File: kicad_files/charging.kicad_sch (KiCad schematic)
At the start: 40 parts, among them Q1 AO3400A, Q2 AO3400A, Q3 AO3401A, Q5 Q_PMOS, Q6 AO3401A, U2 BQ24172RGYR, U3 CYPD3177-24LQ

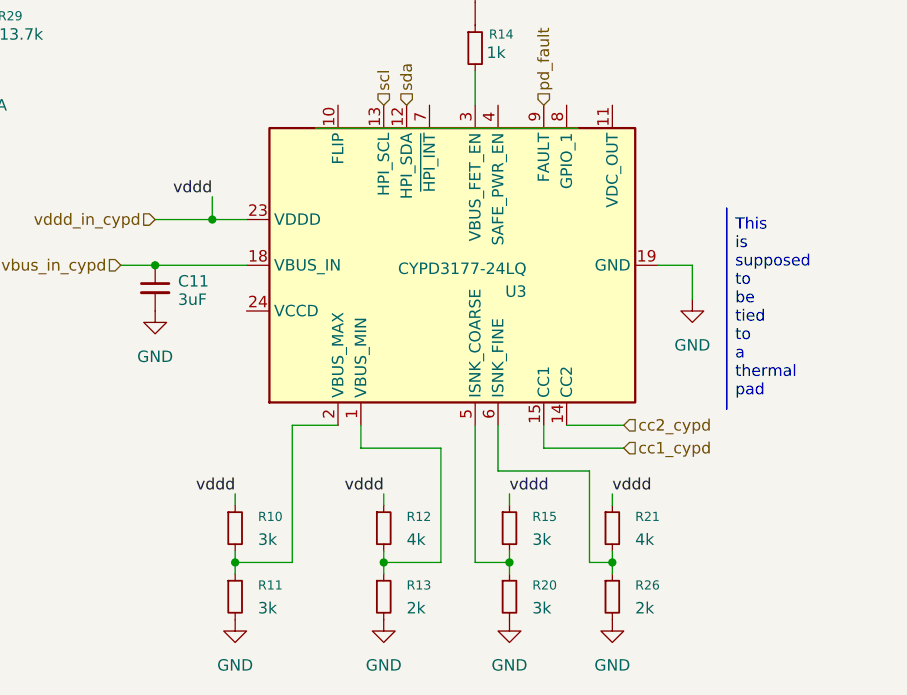
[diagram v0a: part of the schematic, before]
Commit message: fixed some labels and added some passives
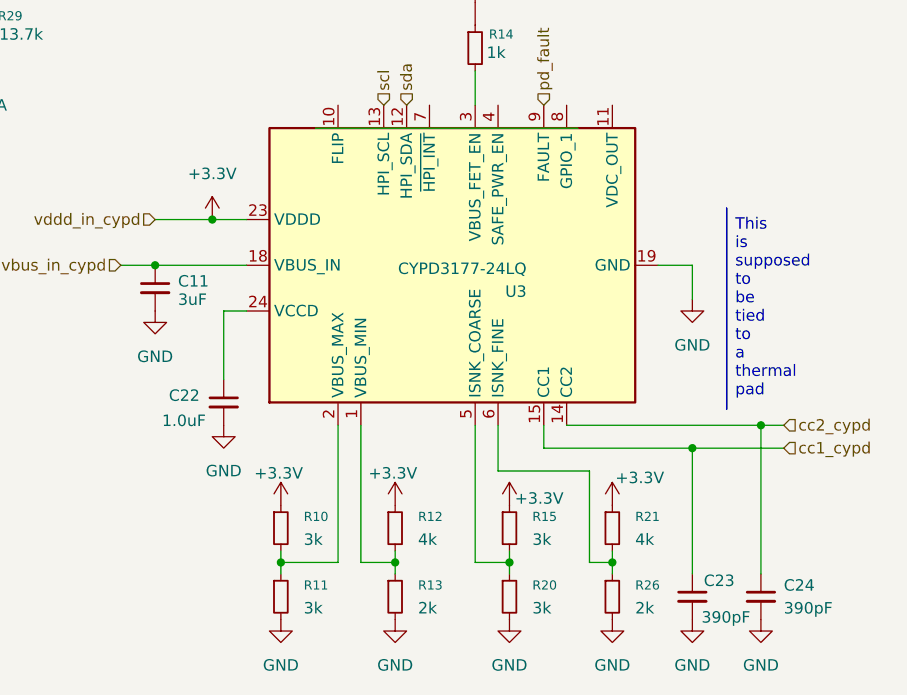
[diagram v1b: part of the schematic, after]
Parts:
- added C22: 1.0uF, symbol C_Small:C_Small
- added C23, C24: 390pF, symbol C_Small:C_Small
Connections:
- net GND: now also C22.2, C23.2, C24.2
- net cc1_cypd: now also C23.1
- net cc2_cypd: now also C24.1
- net at U3.24 (VCCD): now also C22.1
- net vddd_in_cypd renamed +3.3V
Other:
- moved on the sheet: R10, R11, R12, R13

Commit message: copying from reference
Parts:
- added R34: R_Small, symbol R_Small:R_Small
- Q5: value Q_PMOS -> DMP3013
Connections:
- net at Q5.G: no longer R14.1
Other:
- moved on the sheet: Q5, R14
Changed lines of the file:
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@@
 	(wire
 		(pts
-			(xy 237.49 95.25) (xy 237.49 99.06)
+			(xy 237.49 96.52) (xy 237.49 99.06)
 		)
 		(stroke
@@
 	(hierarchical_label "chg_out_cypd"
 		(shape input)
-		(at 242.57 82.55 0)
+		(at 251.46 68.58 0)
 		(effects
 			(font
@@
 	)
 	(symbol
+		(lib_id "R_Small:R_Small")
+		(at 237.49 82.55 0)
+		(unit 1)
+		(body_style 1)
+		(exclude_from_sim no)
+		(in_bom yes)
+		(on_board yes)
+		(in_pos_files yes)
+		(dnp no)
+		(fields_autoplaced yes)
+		(property "Reference" "R34"
+			(at 240.03 81.2799 0)
+			(show_name no)
+			(do_not_autoplace no)
+			(effects
+				(font
+					(size 1.016 1.016)
+				)
+				(justify left)
+			)
+		)
+		(property "Value" "R_Small"
+			(at 240.03 83.8199 0)
+			(show_name no)
+			(do_not_autoplace no)
+			(effects
+				(font
+					(size 1.27 1.27)
+				)
+				(justify left)
+			)
+		)
+		(property "Footprint" ""
+			(at 237.49 82.55 0)
+			(hide yes)
+			(show_name no)
+			(do_not_autoplace no)
+			(effects
+				(font
+					(size 1.27 1.27)
+				)
+			)
+		)
+		(property "Datasheet" ""
+			(at 237.49 82.55 0)
+			(hide yes)
+			(show_name no)
+			(do_not_autoplace no)
+			(effects
+				(font
+					(size 1.27 1.27)
+				)
+			)
+		)
+		(property "Description" "Resistor, small symbol"
+			(at 237.49 82.55 0)
+			(hide yes)
+			(show_name no)
+			(do_not_autoplace no)
+			(effects
+				(font
+					(size 1.27 1.27)
+				)
+			)
+		)
+		(pin "2"
+		)
+		(pin "1"
+		)
+		(instances
+			(project "sodiumBMS"
+				(path "/fcdd2084-f4ec-4b1b-b9ac-497c327c0303/6e36d9cc-6a8c-4543-ae7a-077a6a363a91"
+					(reference "R34")
+					(unit 1)
+				)
+			)
+		)
+	)
+	(symbol
 		(lib_id "Device:C_Small")
 		(at 78.74 54.61 0)
@@
 	(symbol
 		(lib_id "Q_PMOS:Q_PMOS")
-		(at 237.49 85.09 90)
+		(at 246.38 71.12 90)
 		(unit 1)
 		(body_style 1)
@@
 		(fields_autoplaced yes)
 		(property "Reference" "Q5"
-			(at 237.49 76.2 90)
+			(at 246.38 62.23 90)
 			(show_name no)
 			(do_not_autoplace no)
@@
 			)
 		)
-		(property "Value" "Q_PMOS"
-			(at 237.49 78.74 90)
+		(property "Value" "DMP3013"
+			(at 246.38 64.77 90)
 			(show_name no)
 			(do_not_autoplace no)
@@
 		)
 		(property "Footprint" ""
-			(at 234.95 80.01 0)
+			(at 243.84 66.04 0)
 			(hide yes)
 			(show_name no)
@@
 		)
 		(property "Datasheet" ""
-			(at 237.49 85.09 0)
+			(at 246.38 71.12 0)
 			(hide yes)
 			(show_name no)
@@
 		)
 		(property "Description" "P-MOSFET transistor"
-			(at 237.49 85.09 0)
+			(at 246.38 71.12 0)
 			(hide yes)
 			(show_name no)
@@
 	(symbol
 		(lib_id "R_Small:R_Small")
-		(at 237.49 92.71 0)
+		(at 237.49 93.98 0)
 		(unit 1)
 		(body_style 1)
@@
 		(dnp no)
 		(property "Reference" "R14"
-			(at 239.014 91.186 0)
+			(at 233.426 92.456 0)
 			(show_name no)
 			(do_not_autoplace no)
@@
 		)
 		(property "Value" "1k"
-			(at 238.76 93.218 0)
+			(at 233.934 94.488 0)
 			(show_name no)
 			(do_not_autoplace no)
@@
 		)
 		(property "Footprint" ""
-			(at 237.49 92.71 0)
+			(at 237.49 93.98 0)
 			(hide yes)
 			(show_name no)
@@
 		)
 		(property "Datasheet" ""
-			(at 237.49 92.71 0)
+			(at 237.49 93.98 0)
 			(hide yes)
 			(show_name no)
@@
 		)
 		(property "Description" "Resistor, small symbol"
-			(at 237.49 92.71 0)
+			(at 237.49 93.98 0)
 			(hide yes)
 			(show_name no)

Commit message: copying from reference
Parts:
- removed Q5: DMP3013, symbol Q_PMOS:Q_PMOS
- added D1: 15v, symbol D_Zener_Small:D_Zener_Small
- added Q7: DMP3013, symbol Q_PMOS_Depletion:Q_PMOS_Depletion
- added Q8: DMP3013, symbol Q_NMOS_Depletion:Q_NMOS_Depletion
- added R35: 47k, symbol R_Small:R_Small
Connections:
- net at R34.1: now also D1.2 (A), R35.2
- new net: D1.1 (K), Q7.G, Q8.G, R35.1
- new net: Q7.S, Q8.D

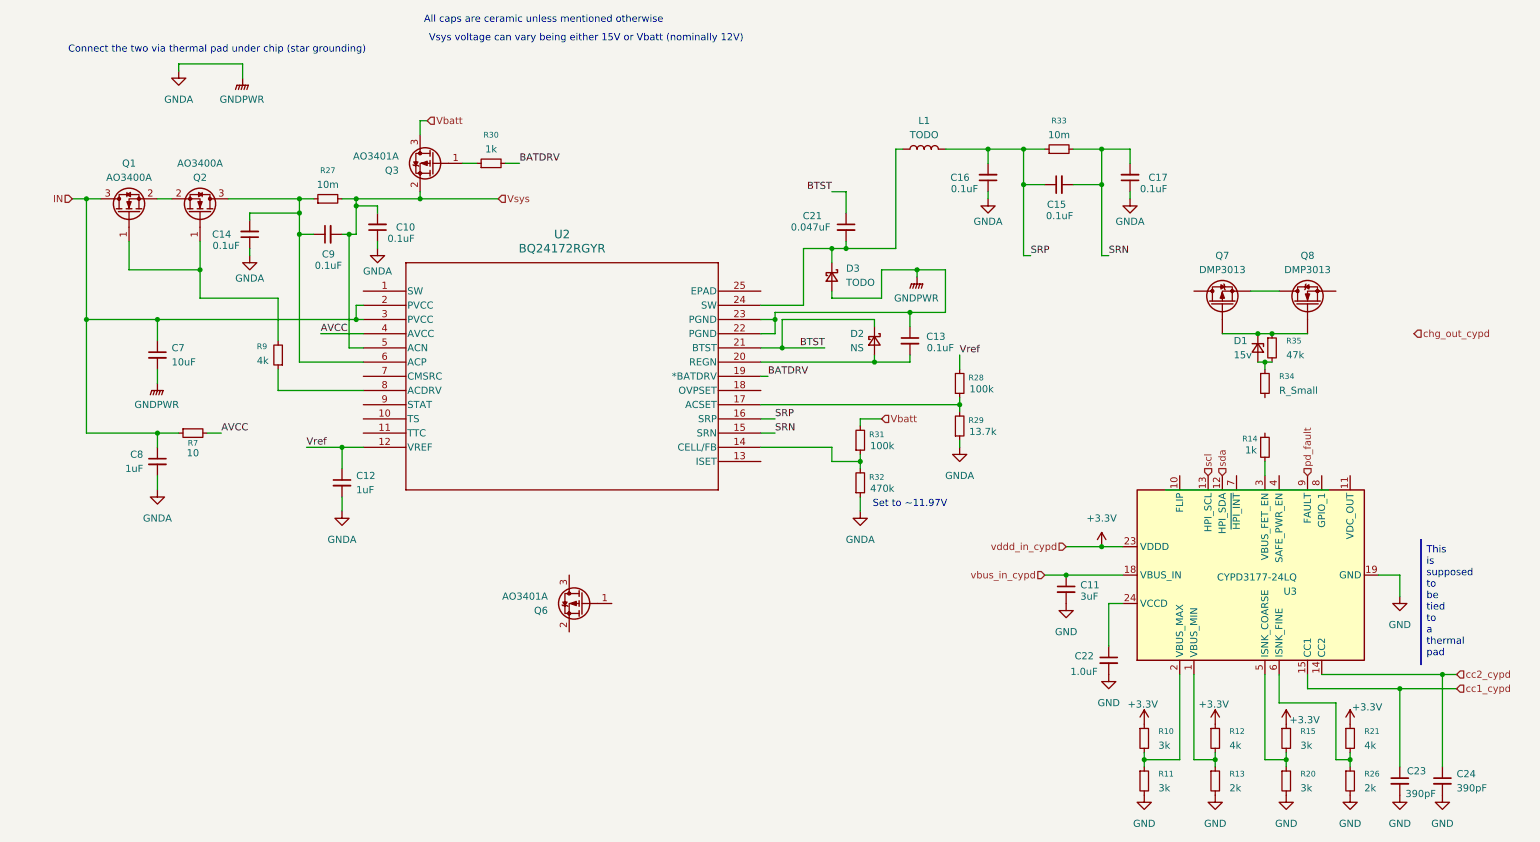
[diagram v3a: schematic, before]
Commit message: Implement circuitry for STAT and TS pins (BQ IC)
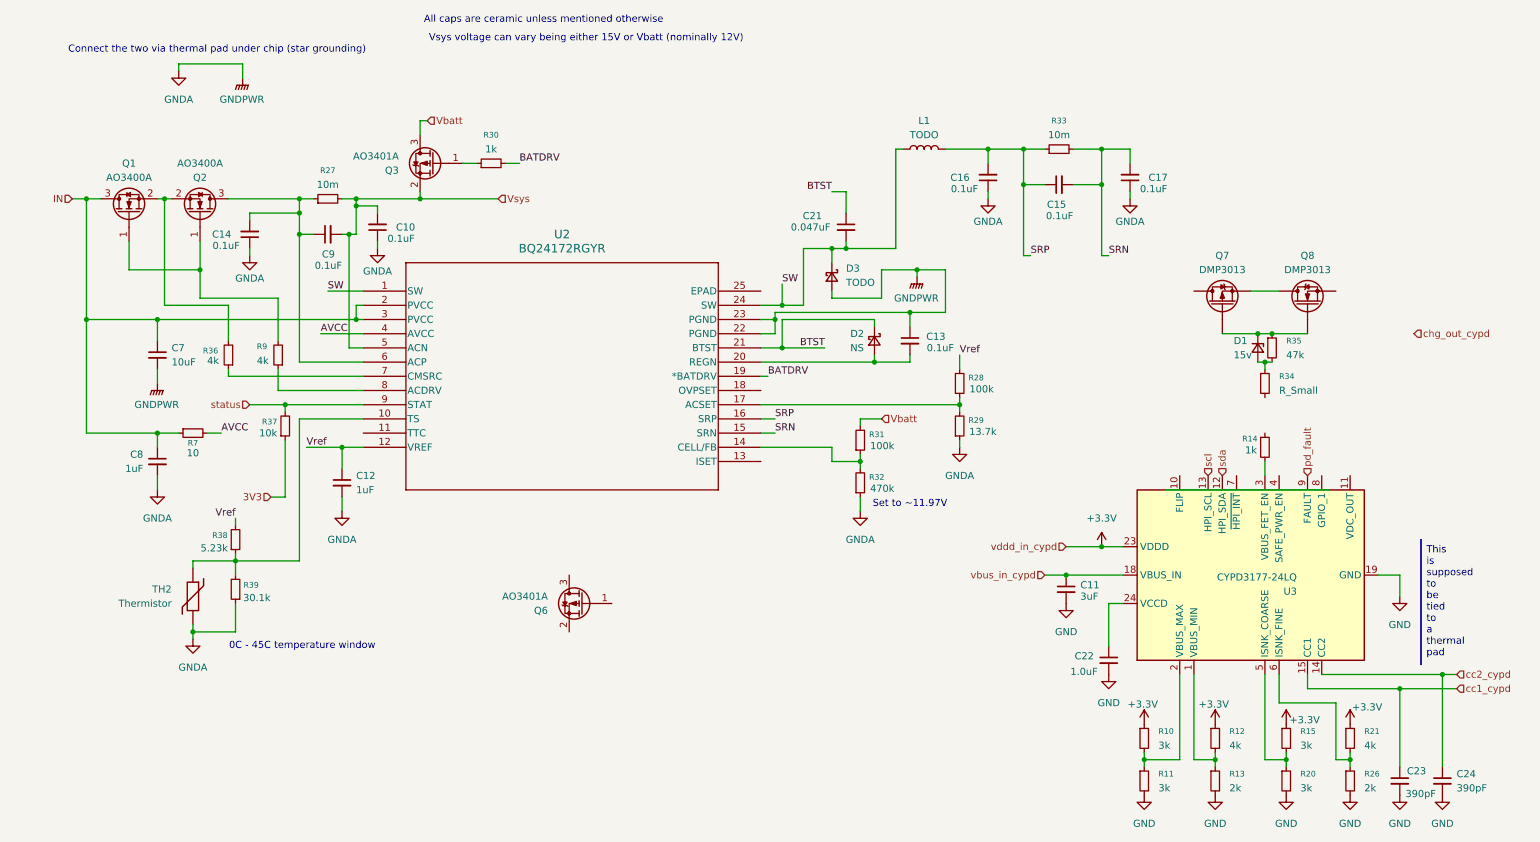
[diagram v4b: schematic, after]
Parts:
- added R36: 4k, symbol Device:R_Small
- added R37: 10k, symbol Device:R_Small
- added R38: 5.23k, symbol Device:R_Small
- added R39: 30.1k, symbol Device:R_Small
- added TH2: Thermistor, symbol Device:Thermistor
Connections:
- net GNDA: now also R39.1, TH2.2
- net Vref: now also R38.2
- net at Q1.2 (S), Q2.2 (S): now also R36.2
- net SW: now reaches C21.2, D3.1 (K), L1.1, U2.24 (SW)
- net SW: now also U2.1 (SW)
- net at U2.10 (TS): now also R38.1, R39.2, TH2.1
- net at U2.7 (CMSRC): now also R36.1
- net status: now reaches U2.9 (STAT)
- net status: now also R37.2
- new net 3V3: R37.1
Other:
- note added: "0C - 45C temperature window"

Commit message: Finally finish BQ24172 schematic
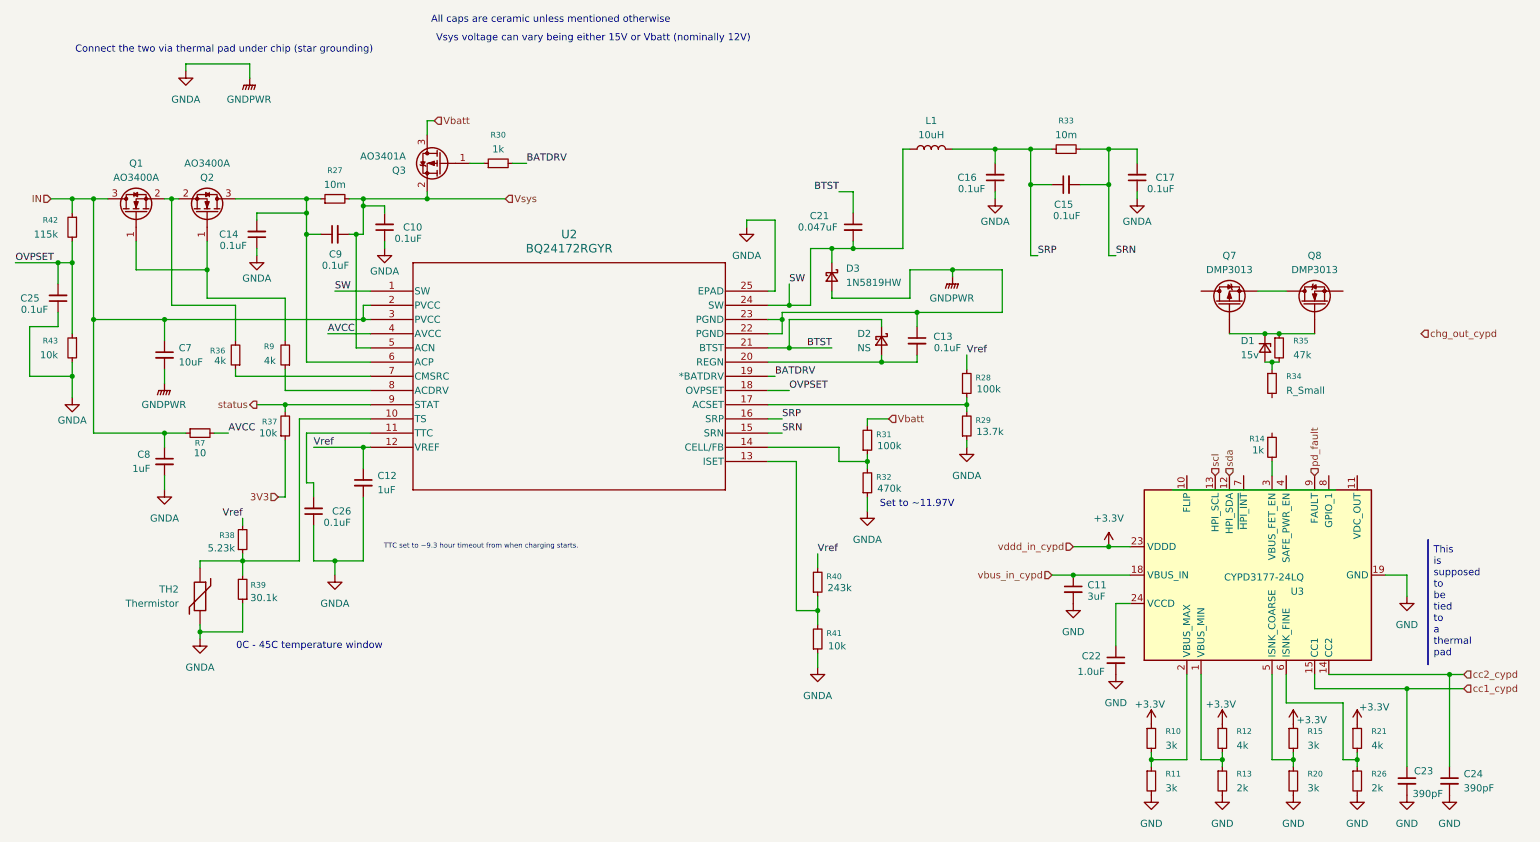
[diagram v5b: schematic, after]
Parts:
- removed Q6: AO3401A, Package_TO_SOT_SMD:SOT-23, symbol Transistor_FET:AO3401A
- added C25, C26: 0.1uF, symbol Device:C_Small
- added R40: 243k, symbol Device:R_Small
- added R41, R43: 10k, symbol Device:R_Small
- added R42: 115k, symbol Device:R_Small
- D3: value TODO -> 1N5819HW
- L1: value TODO -> 10uH
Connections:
- net GNDA: now also U2.25 (EPAD), C25.1, C26.1, R41.1, R43.2
- net IN: now also R42.1
- net Vref: now also R40.2
- net at U2.11 (TTC): now also C26.2
- net at U2.13 (ISET): now also R40.1, R41.2
- net OVPSET: now reaches U2.18 (OVPSET)
- net OVPSET: now also C25.2, R42.2, R43.1
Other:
- note added: "TTC set to ~9.3 hour timeout from when charging starts."
- moved on the sheet: C10, C11, C12, C13, C14, C15, C16, C17, C21, C22, C23, C24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
